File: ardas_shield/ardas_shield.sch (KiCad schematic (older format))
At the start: 37 parts, among them CON1 SD_Card, IC1 DS1307, P1 CONN_10, P10 CONN_01X03, P2 CONN_8, P3 CONN_8, P4 CONN_ICSP, P5 CONN_6, P6 TTL_COMM, P7 CONN_01X03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

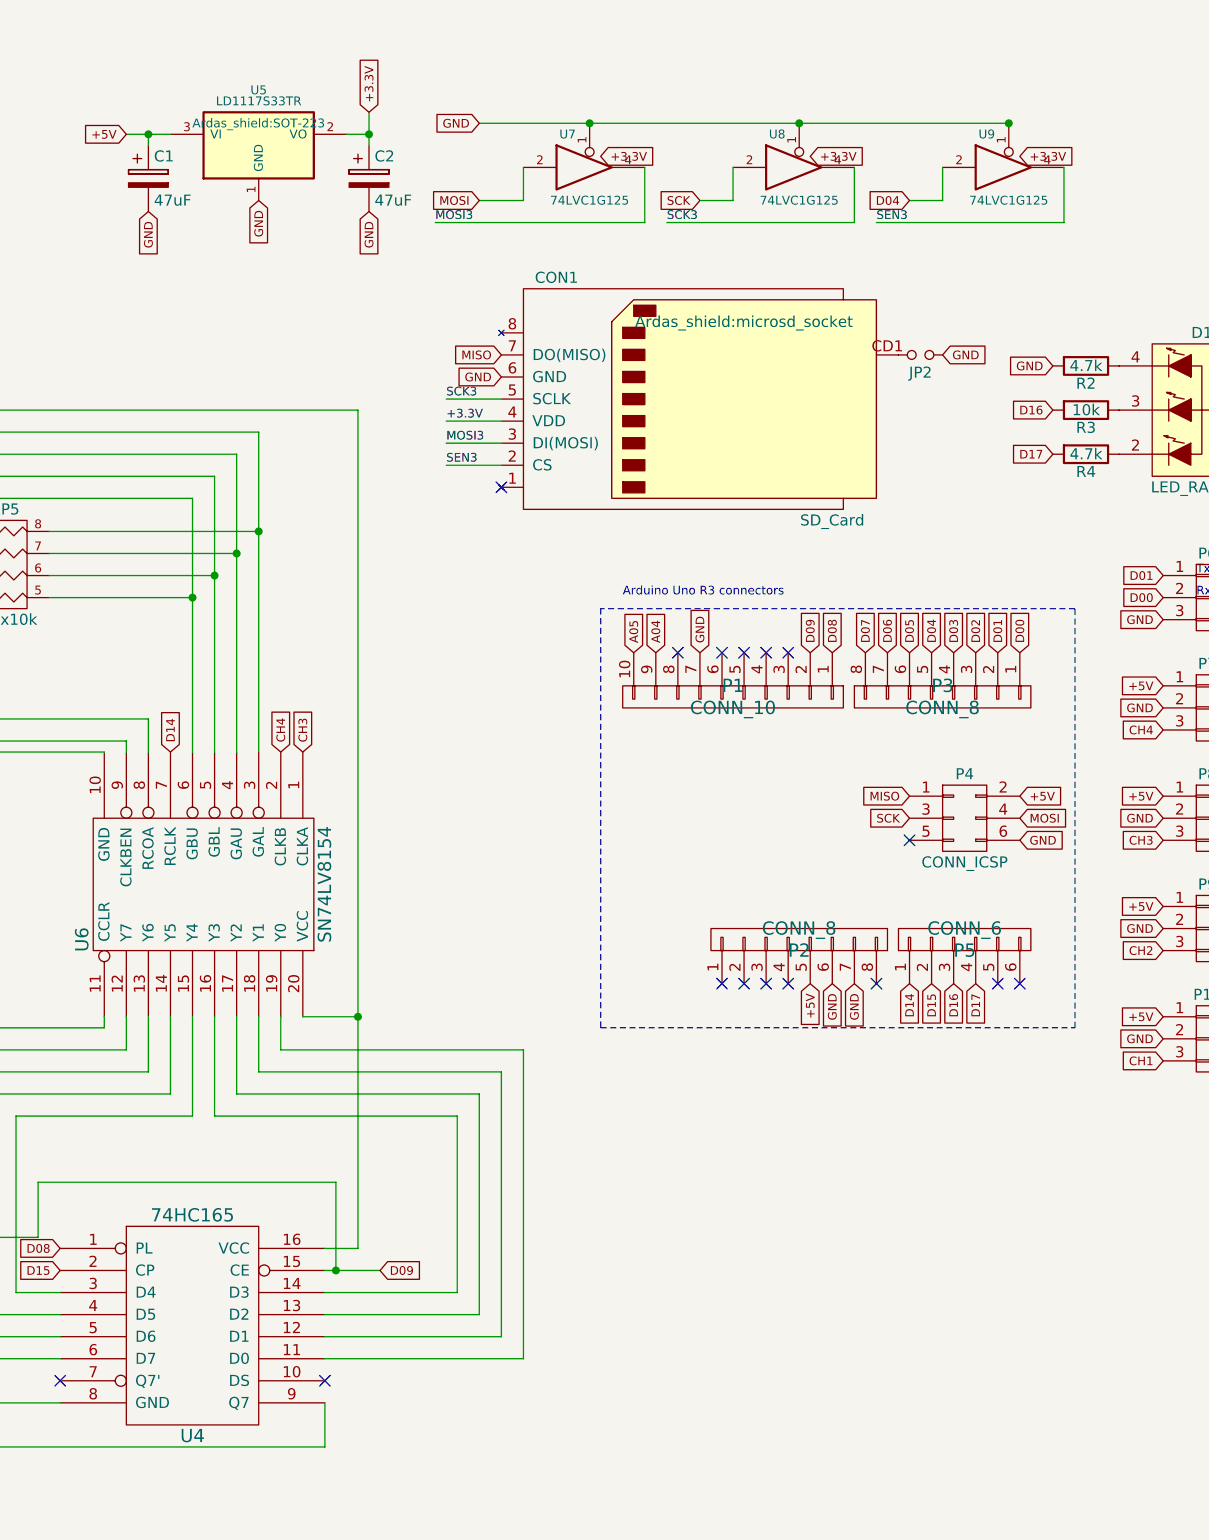
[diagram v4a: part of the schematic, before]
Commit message: updated SD card and RGB-LED
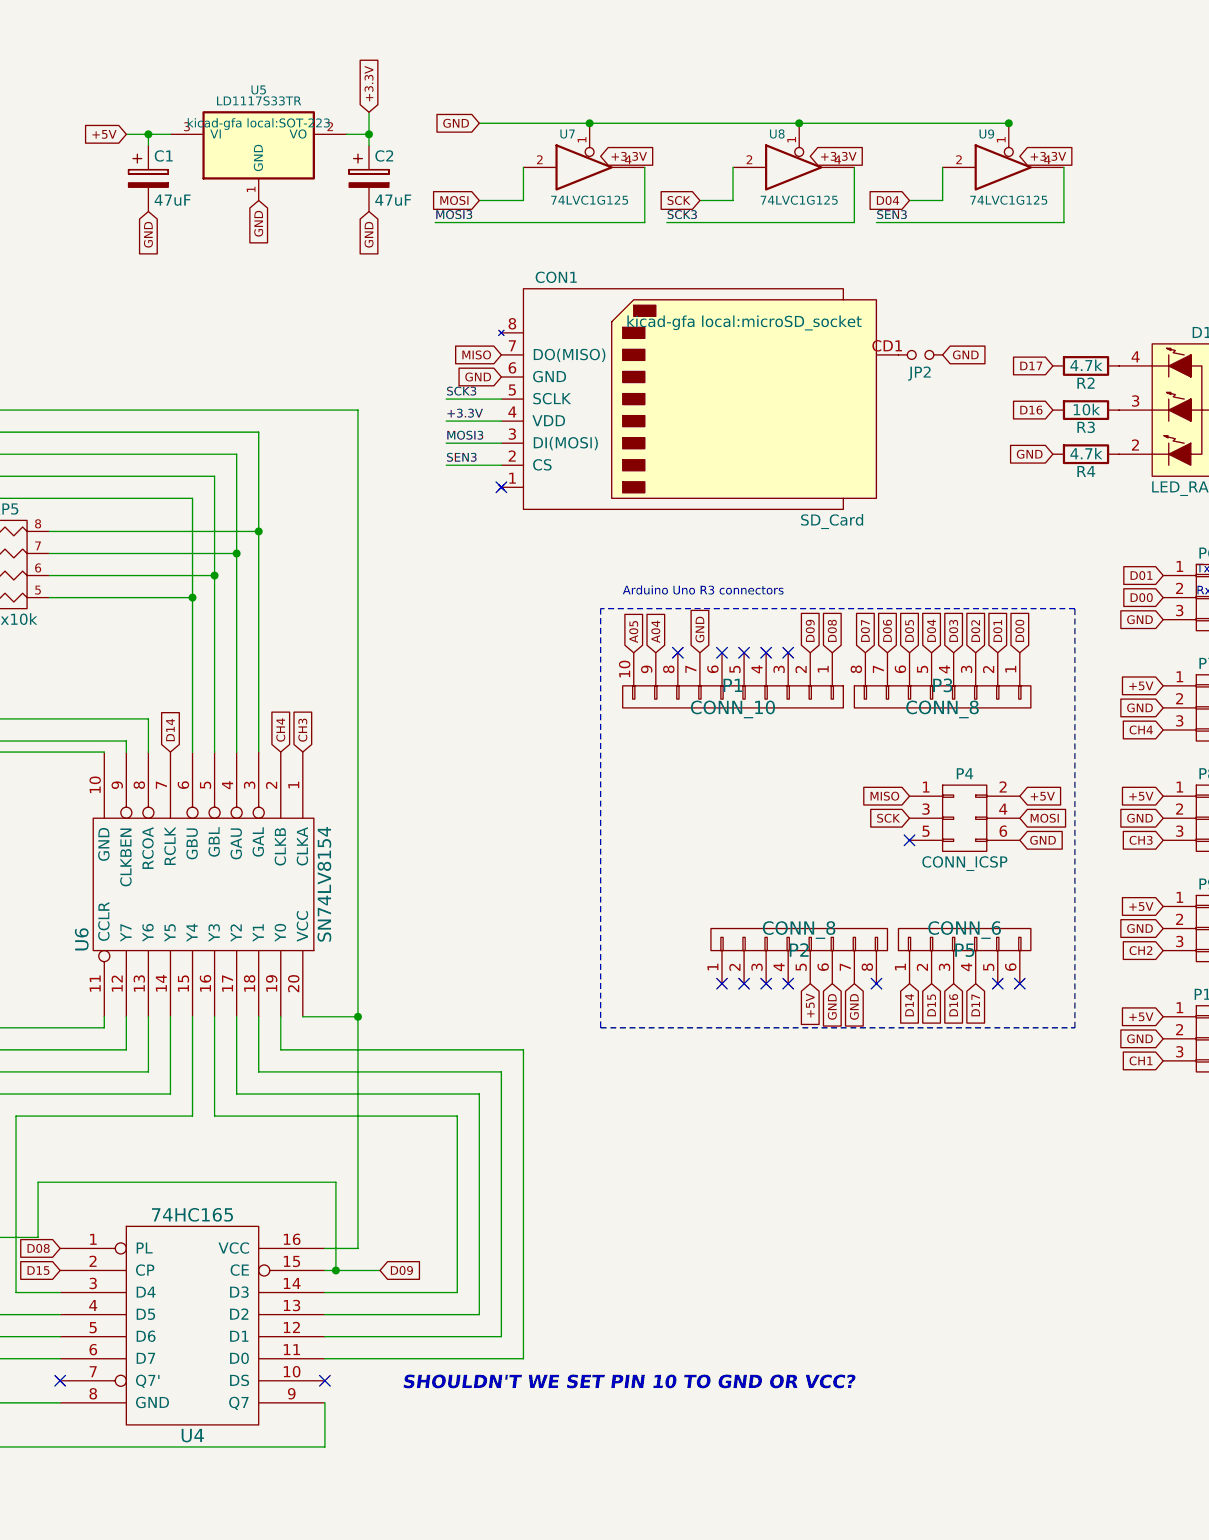
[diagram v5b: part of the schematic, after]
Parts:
- BT1: footprint Ardas_shield:BATTERY_KEYSTONE_12mm -> kicad-gfa local:BATTERY_KEYSTONE_12mm
- C1, C2: footprint Ardas_shield:C_0805 -> kicad-gfa local:C_0805
- CON1: footprint Ardas_shield:microsd_socket -> kicad-gfa local:microSD_socket
- D1: footprint Ardas_shield:led-P-LCC-4-3 -> kicad-gfa local:led-P-LCC-4-3
- IC1: footprint Ardas_shield:SOIC-8-N -> kicad-gfa local:SOIC-8-N
- JP1, JP2: footprint RTC_Ardas_test:small_no_jumper -> kicad-gfa local:small_no_jumper
- P1: footprint Ardas_shield:Pin_Header_Straight_1x10 -> kicad-gfa local:Pin_Header_Straight_1x10
- P10, P6, P7, P8, P9: footprint Ardas_shield:Pin_Header_Angled_1x03 -> kicad-gfa local:Pin_Header_Angled_1x03
- P2, P3: footprint Ardas_shield:Pin_Header_Straight_1x08 -> kicad-gfa local:Pin_Header_Straight_1x08
- P4: footprint Ardas_shield:Socket_Strip_Straight_2x03 -> kicad-gfa local:Socket_Strip_Straight_2x03
- P5: footprint Ardas_shield:Pin_Header_Straight_1x06 -> kicad-gfa local:Pin_Header_Straight_1x06
- R1, R2, R3, R4: footprint Ardas_shield:R_0805 -> kicad-gfa local:R_0805
- U1: footprint Ardas_shield:SOIC-16_7.5x10.3mm_Pitch1.27mm -> kicad-gfa local:SOIC-16_7.5x10.3mm_Pitch1.27mm
- U2, U4: footprint Ardas_shield:SOIC-16_3.9x9.9mm_Pitch1.27mm -> kicad-gfa local:SOIC-16_3.9x9.9mm_Pitch1.27mm
- U3, U6: footprint Ardas_shield:TSSOP-20_4.4x6.5mm_Pitch0.65mm -> kicad-gfa local:TSSOP-20_4.4x6.5mm_Pitch0.65mm
- U5: footprint Ardas_shield:SOT-223 -> kicad-gfa local:SOT-223
- U7, U8, U9: footprint Ardas_shield:SC-70-5 -> kicad-gfa local:SC-70-5
- X1: footprint Ardas_shield:XTAL_ABRACON_ABS07 -> kicad-gfa local:XTAL_ABRACON_ABS07
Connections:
- net D17: now also R2.2; no longer R4.2
- net GND: now also R4.2; no longer R2.2
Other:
- note added: "SHOULDN'T WE SET PIN 10 TO GND OR VCC?"

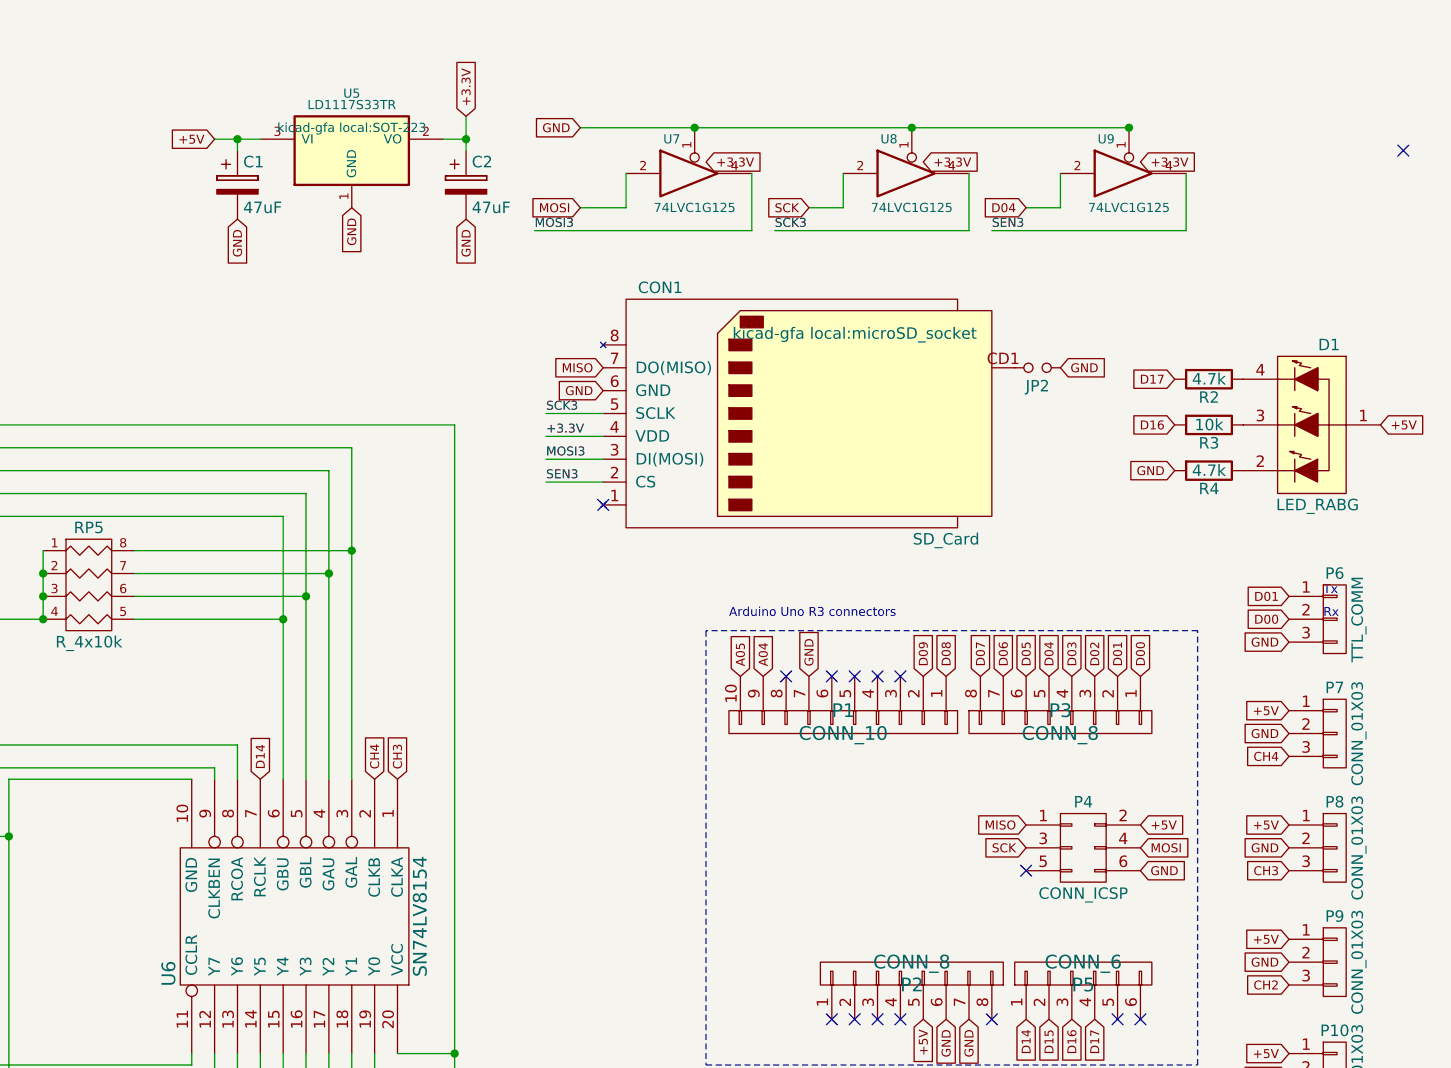
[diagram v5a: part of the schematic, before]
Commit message: remove sd card components
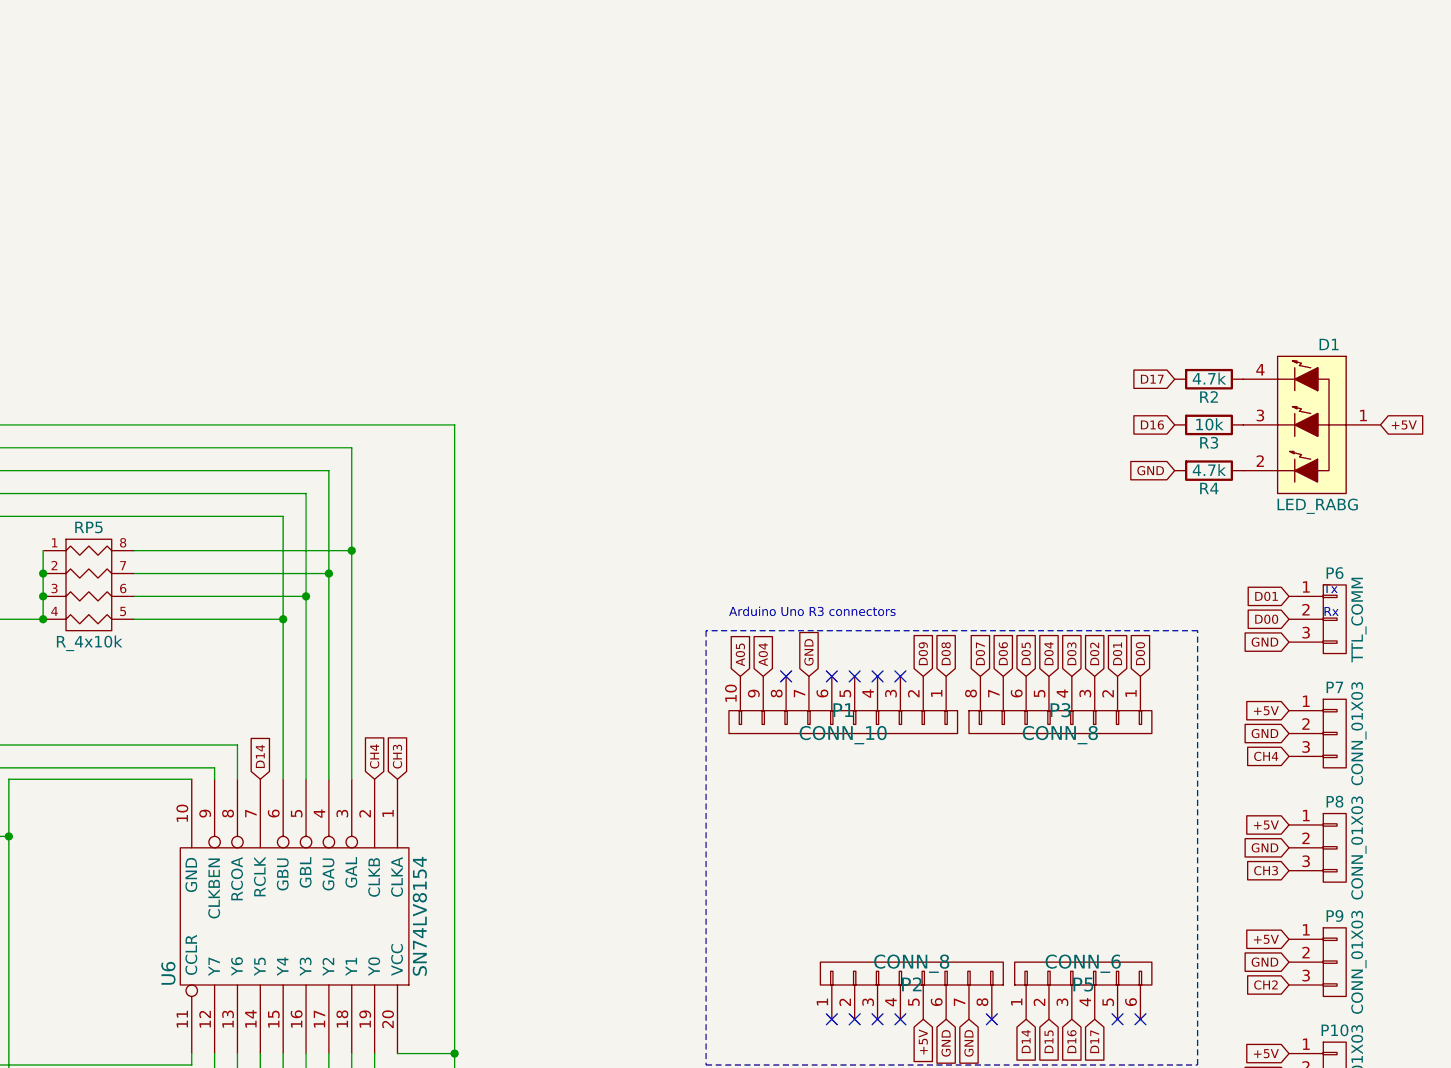
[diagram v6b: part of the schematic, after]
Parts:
- removed C1, C2: 47uF, kicad-gfa local:C_0805, symbol CP
- removed CON1: SD_Card, kicad-gfa local:microSD_socket, symbol SD_Card
- removed JP2: Jumper_NO_Small, kicad-gfa local:small_no_jumper, symbol Jumper_NO_Small
- removed P4: CONN_ICSP, kicad-gfa local:Socket_Strip_Straight_2x03, symbol CONN_02X03
- removed U5: LD1117S33TR, kicad-gfa local:SOT-223, symbol LD1117S33TR
- removed U7, U8, U9: 74LVC1G125, kicad-gfa local:SC-70-5, symbol 74LVC1G125
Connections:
- no-connect marks 20 -> 17
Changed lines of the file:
@@
 	1    0    0    -1
 $EndComp
-Text GLabel 9100 1300 3    39   Input ~ 0
-GND
 Text Notes 10250 3050 0    39   ~ 0
 Arduino Uno R3 connectors
-Text GLabel 8100 1300 3    39   Input ~ 0
-GND
-Text GLabel 9600 900  0    39   Input ~ 0
-GND
-$Comp
-L 74LVC1G125 U7
-U 1 1 56550034
-P 10100 1100
-F 0 "U7" H 10000 1250 40  0000 C CNN
-F 1 "74LVC1G125" H 10100 950 40  0000 C CNN
-F 2 "kicad-gfa local:SC-70-5" H 10100 1100 60  0001 C CNN
-F 3 "" H 10100 1100 60  0000 C CNN
-	1    10100 1100
-	1    0    0    -1
-$EndComp
-$Comp
-L 74LVC1G125 U8
-U 1 1 56550392
-P 11050 1100
-F 0 "U8" H 10950 1250 40  0000 C CNN
-F 1 "74LVC1G125" H 11050 950 40  0000 C CNN
-F 2 "kicad-gfa local:SC-70-5" H 11050 1100 60  0001 C CNN
-F 3 "" H 11050 1100 60  0000 C CNN
-	1    11050 1100
-	1    0    0    -1
-$EndComp
-$Comp
-L 74LVC1G125 U9
-U 1 1 5655048F
-P 12000 1100
-F 0 "U9" H 11900 1250 40  0000 C CNN
-F 1 "74LVC1G125" H 12000 950 40  0000 C CNN
-F 2 "kicad-gfa local:SC-70-5" H 12000 1100 60  0001 C CNN
-F 3 "" H 12000 1100 60  0000 C CNN
-	1    12000 1100
-	1    0    0    -1
-$EndComp
-Text Label 9400 1350 0    39   ~ 0
-MOSI3
-Text Label 10450 1350 0    39   ~ 0
-SCK3
-Text Label 11400 1350 0    39   ~ 0
-SEN3
-Text GLabel 11550 1250 0    39   Input ~ 0
-D04
-$Comp
-L LD1117S33TR U5
-U 1 1 565533AB
-P 8600 1000
-F 0 "U5" H 8600 1250 40  0000 C CNN
-F 1 "LD1117S33TR" H 8600 1200 40  0000 C CNN
-F 2 "kicad-gfa local:SOT-223" H 8600 1100 40  0000 C CNN
-F 3 "https://github.com/UMONS-GFA/kicad-gfa.pretty/blob/master/datasheets/1776449.pdf" H 8600 1000 60  0001 C CNN
-F 4 "1202826" H 8600 1000 60  0001 C CNN "Order_Code"
-F 5 "STMICROELECTRONICS" H 8600 1000 60  0001 C CNN "MFN"
-F 6 " LD1117S33TR" H 8600 1000 60  0001 C CNN "MFP"
-	1    8600 1000
-	1    0    0    -1
-$EndComp
-$Comp
-L CP C1
-U 1 1 565535F2
-P 8100 1150
-F 0 "C1" H 8125 1250 50  0000 L CNN
-F 1 "47uF" H 8125 1050 50  0000 L CNN
-F 2 "kicad-gfa local:C_0805" H 8138 1000 30  0001 C CNN
-F 3 "" H 8100 1150 60  0000 C CNN
-	1    8100 1150
-	1    0    0    -1
-$EndComp
-$Comp
-L CP C2
-U 1 1 565536BD
-P 9100 1150
-F 0 "C2" H 9125 1250 50  0000 L CNN
-F 1 "47uF" H 9125 1050 50  0000 L CNN
-F 2 "kicad-gfa local:C_0805" H 9138 1000 30  0001 C CNN
-F 3 "" H 9100 1150 60  0000 C CNN
-	1    9100 1150
-	1    0    0    -1
-$EndComp
-Text GLabel 8000 950  0    39   Input ~ 0
-+5V
-Text GLabel 9600 1250 0    39   Input ~ 0
-MOSI
-Text GLabel 10600 1250 0    39   Input ~ 0
-SCK
-Text GLabel 9700 1950 0    39   Input ~ 0
-MISO
-Text GLabel 9700 2050 0    39   Input ~ 0
-GND
-Text Label 9450 2150 0    39   ~ 0
-SCK3
-Text Label 9450 2250 0    39   ~ 0
-+3.3V
-Text GLabel 8600 1250 3    39   Input ~ 0
-GND
-Text Label 9450 2350 0    39   ~ 0
-MOSI3
-Text Label 9450 2450 0    39   ~ 0
-SEN3
-$Comp
-L CONN_02X03 P4
-U 1 1 5655BFA8
-P 11800 4050
-F 0 "P4" H 11800 4250 50  0000 C CNN
-F 1 "CONN_ICSP" H 11800 3850 50  0000 C CNN
-F 2 "kicad-gfa local:Socket_Strip_Straight_2x03" H 11800 2850 60  0001 C CNN
-F 3 "" H 11800 2850 60  0000 C CNN
-F 4 "1266033" H 11800 4050 60  0001 C CNN "Order_Code"
-F 5 "TE CONNECTIVITY / AMP " H 11800 4050 60  0001 C CNN "MFN"
-F 6 "5-534206-3" H 11800 4050 60  0001 C CNN "MFP"
-F 7 "2.54mm" H 11800 4050 60  0001 C CNN "Pitch_Spacing"
-F 8 "Through Hole" H 11800 4050 60  0001 C CNN "Contact_Termination_Type"
-F 9 "Receptacle" H 11800 4050 60  0001 C CNN "Gender"
-	1    11800 4050
-	1    0    0    -1
-$EndComp
-Text GLabel 12050 3950 2    39   Input ~ 0
-+5V
-Text GLabel 11550 3950 0    39   Input ~ 0
-MISO
-Text GLabel 11550 4050 0    39   Input ~ 0
-SCK
-Text GLabel 12050 4050 2    39   Input ~ 0
-MOSI
-Text GLabel 12050 4150 2    39   Input ~ 0
-GND
-NoConn ~ 9700 2550
 Text Notes 12850 3050 0    39   ~ 0
 Rx
@@
 	1    0    0    1
 $EndComp
-NoConn ~ 11550 4150
 $Comp
 L GND #PWR04
@@
 	1    0    0    -1
 $EndComp
-Text GLabel 11100 1050 2    39   Input ~ 0
-+3.3V
-Text GLabel 12050 1050 2    39   Input ~ 0
-+3.3V
 $Comp
 L Battery BT1
@@
 NoConn ~ 4600 2100
 NoConn ~ 2000 4200
-NoConn ~ 13200 1000
-$Comp
-L SD_Card CON1
-U 1 1 5655FE06
-P 10600 2150
-F 0 "CON1" H 9950 2700 50  0000 C CNN
-F 1 "SD_Card" H 11200 1600 50  0000 C CNN
-F 2 "kicad-gfa local:microSD_socket" H 10800 2500 50  0000 C CNN
-F 3 "https://github.com/UMONS-GFA/kicad-gfa.pretty/blob/master/datasheets/1717993.pdf" H 10600 2150 60  0001 C CNN
-F 4 "2334075" H 10600 2150 60  0001 C CNN "Order_Code"
-F 5 "MOLEX" H 10600 2150 60  0001 C CNN "MFN"
-F 6 "503182-1853" H 10600 2150 60  0001 C CNN "MFP"
-	1    10600 2150
-	1    0    0    -1
-$EndComp
 Wire Wire Line
 	5300 1600 5300 2600
@@
 Wire Notes Line
 	12300 5000 12300 3100
-Wire Wire Line
-	9700 2150 9450 2150
-Wire Wire Line
-	9700 2250 9450 2250
-Wire Wire Line
-	11700 1250 11550 1250
-Wire Wire Line
-	10750 1250 10600 1250
-Wire Wire Line
-	9800 1250 9600 1250
-Connection ~ 8100 950
-Wire Wire Line
-	8000 950  8200 950
-Wire Wire Line
-	8100 1000 8100 950
-Connection ~ 9100 950
-Wire Wire Line
-	9100 850  9100 1000
-Wire Wire Line
-	9000 950  9100 950
-Wire Wire Line
-	10350 1350 10350 1100
-Wire Wire Line
-	9400 1350 10350 1350
-Wire Wire Line
-	9800 1100 9800 1250
-Wire Wire Line
-	12250 1350 12250 1100
-Wire Wire Line
-	11400 1350 12250 1350
-Wire Wire Line
-	11700 1100 11700 1250
-Wire Wire Line
-	11300 1350 10450 1350
-Wire Wire Line
-	11300 1100 11300 1350
-Wire Wire Line
-	10750 1100 10750 1250
-Connection ~ 11050 900
-Connection ~ 10100 900
 Wire Notes Line
 	10150 3100 10150 5000
@@
 Connection ~ 6950 4300
 Connection ~ 6950 4000
-Connection ~ 12000 900
-Wire Wire Line
-	9600 900  12000 900
 Wire Wire Line
 	6950 4000 6950 4300
@@
 NoConn ~ 11950 4800
 NoConn ~ 12050 4800
-$Comp
-L Jumper_NO_Small JP2
-U 1 1 569E9D5A
-P 11600 1950
-F 0 "JP2" H 11600 2030 50  0000 C CNN
-F 1 "Jumper_NO_Small" H 11610 1890 50  0001 C CNN
-F 2 "kicad-gfa local:small_no_jumper" H 11600 1950 50  0001 C CNN
-F 3 "" H 11600 1950 50  0000 C CNN
-	1    11600 1950
-	-1   0    0    1
-$EndComp
-Text GLabel 11700 1950 2    39   Input ~ 0
-GND
-Wire Wire Line
-	9700 2350 9450 2350
-Wire Wire Line
-	9700 2450 9450 2450
-Text GLabel 10150 1050 2    39   Input ~ 0
-+3.3V
-Text GLabel 9100 850  1    39   Input ~ 0
-+3.3V
 Text Notes 9250 6650 0    60   Italic 12
 SHOULDN'T WE SET PIN 10 TO GND OR VCC?
